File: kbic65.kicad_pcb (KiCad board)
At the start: 2 copper layers, 141 parts, among them U1 ProMicro

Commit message: Added and updated footprints
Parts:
- added MX_BKSLSH2(ISO_Enter): MX-NoLED, MX_Only:MXOnly-ISO-ROTATED-ReversedStabilizers-NoLED, F.Cu at (287.3, 60.3)
- added MX_CpsLck2: MX-NoLED, MX_Only:MXOnly-1.25U-NoLED, F.Cu at (25.4, 69.8)
- added MX_Enter2(ISO_Hash): MX-NoLED, MX_Only:MXOnly-1U-NoLED, F.Cu at (265.9, 69.8)
- added MX_LShift2: MX-NoLED, MX_Only:MXOnly-2.25U-NoLED, F.Cu at (34.9, 88.9)
- added MX_RAlt2: MX-NoLED, MX_Only:MXOnly-1.25U-NoLED, F.Cu at (211.1, 108.0)
- added MX_RAlt3: MX-NoLED, MX_Only:MXOnly-1.25U-NoLED, F.Cu at (215.9, 108.0)
- added MX_RWin2(RCtrl2): MX-NoLED, MX_Only:MXOnly-1.25U-NoLED, F.Cu at (239.7, 108.0)
- added MX_Space2: MX-NoLED, MX_Only:MXOnly-6U-Centered-NoLED, F.Cu at (142.1, 108.0)
- MX_BKSLSH1: footprint MX_Only:MXOnly-1U-NoLED -> MX_Only:MXOnly-1.5U-NoLED
- MX_Enter1: footprint MX_Only:MXOnly-1U-NoLED -> MX_Only:MXOnly-2.25U-NoLED

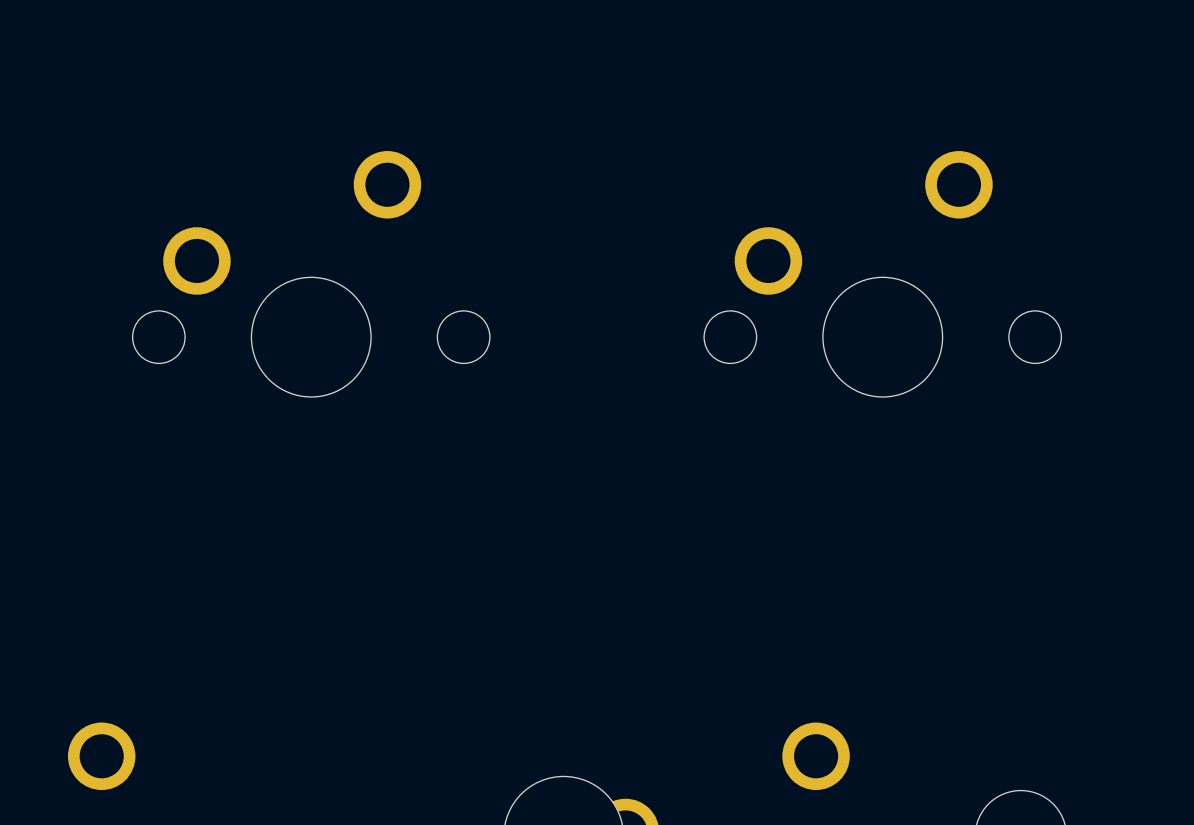
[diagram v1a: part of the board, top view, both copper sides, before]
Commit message: Added and updated footprints
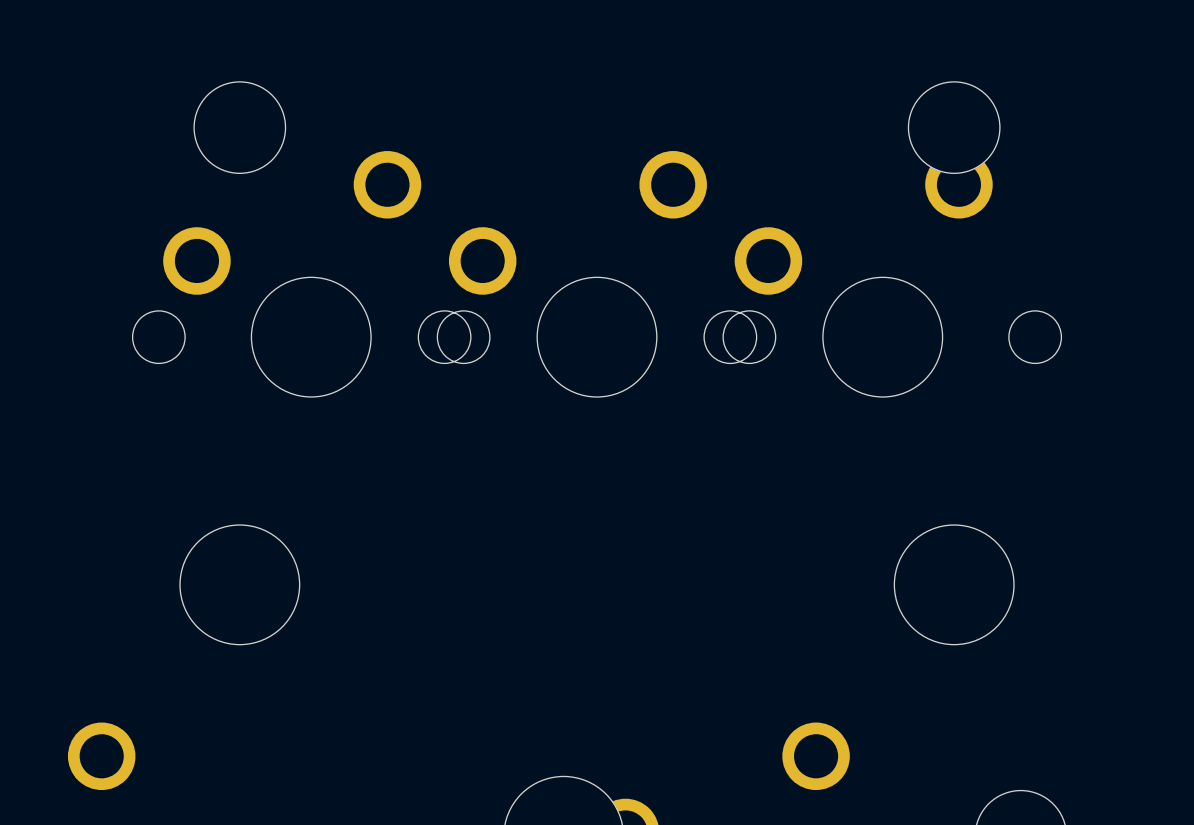
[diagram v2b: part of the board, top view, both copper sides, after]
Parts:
- added MX_BkSp2(RegBkSp): MX-NoLED, MX_Only:MXOnly-2U-NoLED, F.Cu at (280.2, 31.8)
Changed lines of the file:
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@@
     (tracks 0)
     (zones 0)
-    (modules 149)
+    (modules 150)
     (nets 95)
   )
@@
     (add_net ROW8)
   )
+  (module MX_Only:MXOnly-2U-NoLED (layer F.Cu)
+    (at 280.19375 31.75)
+    (fp_text reference "MX_BkSp2(RegBkSp)" (at 0 3.175) (layer Dwgs.User)
+      (effects (font (size 1 1) (thickness 0.15)))
+    )
+    (fp_text value MX-NoLED (at 0 -7.9375) (layer Dwgs.User)
+      (effects (font (size 1 1) (thickness 0.15)))
+    )
+    (fp_line (start -19.05 9.525) (end -19.05 -9.525) (layer Dwgs.User) (width 0.15))
+    (fp_line (start -19.05 9.525) (end 19.05 9.525) (layer Dwgs.User) (width 0.15))
+    (fp_line (start 19.05 -9.525) (end 19.05 9.525) (layer Dwgs.User) (width 0.15))
+    (fp_line (start -19.05 -9.525) (end 19.05 -9.525) (layer Dwgs.User) (width 0.15))
+    (fp_line (start -7 -7) (end -7 -5) (layer Dwgs.User) (width 0.15))
+    (fp_line (start -5 -7) (end -7 -7) (layer Dwgs.User) (width 0.15))
+    (fp_line (start -7 7) (end -5 7) (layer Dwgs.User) (width 0.15))
+    (fp_line (start -7 5) (end -7 7) (layer Dwgs.User) (width 0.15))
+    (fp_line (start 7 7) (end 7 5) (layer Dwgs.User) (width 0.15))
+    (fp_line (start 5 7) (end 7 7) (layer Dwgs.User) (width 0.15))
+    (fp_line (start 7 -7) (end 7 -5) (layer Dwgs.User) (width 0.15))
+    (fp_line (start 5 -7) (end 7 -7) (layer Dwgs.User) (width 0.15))
+    (pad 2 thru_hole circle (at 2.54 -5.08) (size 2.25 2.25) (drill 1.47) (layers *.Cu B.Mask)
+      (net 20 "Net-(D_BkSp1-Pad2)"))
+    (pad "" np_thru_hole circle (at 0 0) (size 3.9878 3.9878) (drill 3.9878) (layers *.Cu *.Mask))
+    (pad 1 thru_hole circle (at -3.81 -2.54) (size 2.25 2.25) (drill 1.47) (layers *.Cu B.Mask)
+      (net 86 COL6))
+    (pad "" np_thru_hole circle (at -5.08 0 48.0996) (size 1.75 1.75) (drill 1.75) (layers *.Cu *.Mask))
+    (pad "" np_thru_hole circle (at 5.08 0 48.0996) (size 1.75 1.75) (drill 1.75) (layers *.Cu *.Mask))
+    (pad "" np_thru_hole circle (at -11.90625 -6.985) (size 3.048 3.048) (drill 3.048) (layers *.Cu *.Mask))
+    (pad "" np_thru_hole circle (at 11.90625 -6.985) (size 3.048 3.048) (drill 3.048) (layers *.Cu *.Mask))
+    (pad "" np_thru_hole circle (at -11.90625 8.255) (size 3.9878 3.9878) (drill 3.9878) (layers *.Cu *.Mask))
+    (pad "" np_thru_hole circle (at 11.90625 8.255) (size 3.9878 3.9878) (drill 3.9878) (layers *.Cu *.Mask))
+  )
   (module MX_Only:MXOnly-ISO-ROTATED-ReversedStabilizers-NoLED (layer F.Cu)

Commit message: Redrew schematic with all extra footprints
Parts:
- renumbered MX_CpsLck2 to MX_CpsLck2(Stepped), MX_LShift2 to MX_LShift2(ANSI)
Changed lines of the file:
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@@
   (module MX_Only:MXOnly-1.25U-NoLED (layer F.Cu)
     (at 25.4 69.85)
-    (fp_text reference MX_CpsLck2 (at 0 3.175) (layer Dwgs.User)
+    (fp_text reference "MX_CpsLck2(Stepped)" (at 0 3.175) (layer Dwgs.User)
       (effects (font (size 1 1) (thickness 0.15)))
     )
@@
   (module MX_Only:MXOnly-2.25U-NoLED (layer F.Cu)
     (at 34.925 88.9)
-    (fp_text reference MX_LShift2 (at 0 3.175) (layer Dwgs.User)
+    (fp_text reference "MX_LShift2(ANSI)" (at 0 3.175) (layer Dwgs.User)
       (effects (font (size 1 1) (thickness 0.15)))
     )

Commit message: Changed layout to top windows and rearranging diodes
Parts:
- removed MX_BKSLSH2(ISO_Enter): MX-NoLED, MX_Only:MXOnly-ISO-ROTATED-ReversedStabilizers-NoLED
- removed MX_BkSp2(RegBkSp): MX-NoLED, MX_Only:MXOnly-2U-NoLED
- removed MX_CpsLck2(Stepped), MX_LShift1, MX_RAlt2, MX_RAlt3, MX_RWin2(RCtrl2): MX-NoLED, MX_Only:MXOnly-1.25U-NoLED
- removed MX_Enter2(ISO_Hash), MX_RAlt1: MX-NoLED, MX_Only:MXOnly-1U-NoLED
- removed MX_LShift2(ANSI): MX-NoLED, MX_Only:MXOnly-2.25U-NoLED
- removed MX_Space1: MX-NoLED, MX_Only:MXOnly-6.25U-NoLED
- removed MX_Space2: MX-NoLED, MX_Only:MXOnly-6U-Centered-NoLED
- added MX_BkSlash2_ISO_Enter1: MX-NoLED, MX_Only:MXOnly-ISO-ROTATED-ReversedStabilizers-NoLED, F.Cu at (346.1, 98.4)
- added MX_BkSp3_2u1: MX-NoLED, MX_Only:MXOnly-2U-NoLED, F.Cu at (338.9, 69.8)
- added MX_CpsLck2_Stepped1: MX-NoLED, MX_Only:MXOnly-1.25U-NoLED, F.Cu at (84.1, 108.0)
- added MX_Enter2_ISO_Hash1: MX-NoLED, MX_Only:MXOnly-1U-NoLED, F.Cu at (324.6, 108.0)
- added MX_LShift_ANSI1: MX-NoLED, MX_Only:MXOnly-2.25U-NoLED, F.Cu at (93.7, 127.0)
- added MX_LShift_ISO1: MX-NoLED, MX_Only:MXOnly-1.25U-NoLED, F.Cu at (84.1, 127.0)
- added MX_RAlt1_1u1: MX-NoLED, MX_Only:MXOnly-1U-NoLED, F.Cu at (272.3, 146.1)
- added MX_RAlt2_1.25u_6u_space1: MX-NoLED, MX_Only:MXOnly-1.25U-NoLED, F.Cu at (269.9, 146.1)
- added MX_RAlt3_1.25u_6.25u_space1: MX-NoLED, MX_Only:MXOnly-1.25U-NoLED, F.Cu at (274.6, 146.1)
- added MX_RWin2_1.25u_RCtrl1: MX-NoLED, MX_Only:MXOnly-1U-NoLED, F.Cu at (298.4, 146.1)
- added MX_Space1_6.25u1: MX-NoLED, MX_Only:MXOnly-6.25U-NoLED, F.Cu at (203.2, 146.1)
- added MX_Space2_6u1: MX-NoLED, MX_Only:MXOnly-6U-Centered-NoLED, F.Cu at (200.8, 146.1)
- moved D_PgDn1 424.5 mm to (396.9, 31.8), turned to 270 degrees
- moved D_Right1 419.5 mm to (401.6, 31.8), turned to 270 degrees
- moved D_PgUp1 416.6 mm to (392.1, 31.8), turned to 270 degrees
- moved D_Del1 401.9 mm to (387.4, 31.8), turned to 270 degrees
- moved D_Up1 387.2 mm to (368.3, 31.8), turned to 270 degrees
- moved D_Down1 381.8 mm to (373.1, 31.8), turned to 270 degrees
- moved D_Tilde1 375.8 mm to (382.6, 31.8), turned to 270 degrees
- moved D_Enter1 370.7 mm to (331.6, -10.5), turned to 270 degrees
- moved D_BKSLSH1 368.3 mm to (363.5, 31.8), turned to 270 degrees
- moved D_SemiCol1 368.2 mm to (327.8, -10.5), turned to 270 degrees
- moved D_K1 365.8 mm to (324.0, -10.5), turned to 270 degrees
- moved D_H1 363.4 mm to (320.2, -10.5), turned to 270 degrees
- moved D_@1 362.3 mm to (327.8, -20.3), turned to 270 degrees
- moved D_F1 361.1 mm to (316.4, -10.5), turned to 270 degrees
- moved D_L1 359.6 mm to (324.0, -20.3), turned to 270 degrees
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- renumbered MX_BKSLSH1 to MX_BkSlsh1

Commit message: Changed diode to row2col instead to make better wiring, rearranging diode footprints
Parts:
- moved D_1 221.6 mm to (110.3, 47.6)
- moved D_Tab1 202.5 mm to (122.2, 47.6)
- moved D_A1 194.8 mm to (126.2, 47.6)
- moved D_3 194.1 mm to (146.1, 46.0)
- moved D_Esc1 188.0 mm to (114.3, 47.6)
- moved D_CpsLck1 187.8 mm to (130.2, 47.6)
- moved D_Q1 183.8 mm to (118.3, 47.6)
- moved D_ISO_BKSLSH1 179.6 mm to (134.1, 47.6)
- moved D_W1 172.7 mm to (158.0, 46.0)
- moved D_5 167.6 mm to (181.8, 43.7)
- moved D_D1 164.6 mm to (161.9, 46.0)
- moved D_2 160.8 mm to (150.0, 46.0)
- moved D_S1 157.2 mm to (165.9, 46.0)
- moved D_E1 155.6 mm to (154.0, 46.0)
- moved D_X1 148.6 mm to (169.9, 46.0)
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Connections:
- D_0 pad 1: ROW1 -> COL5
- D_1 pad 1: ROW0 -> COL0
- D_2 pad 1: ROW1 -> COL1
- D_3 pad 1: ROW0 -> COL1
- D_4 pad 1: ROW1 -> COL2
- D_5 pad 1: ROW0 -> COL2
- D_6 pad 1: ROW1 -> COL3
- D_7 pad 1: ROW0 -> COL3
- D_8 pad 1: ROW1 -> COL4
- D_9 pad 1: ROW0 -> COL4
- D_@1 pad 1: ROW4 -> COL5
- D_A1 pad 1: ROW4 -> COL0
- D_B1 pad 1: ROW7 -> COL3
- D_BKSLSH1 pad 1: ROW2 -> COL6
- D_BkSp1 pad 1: ROW0 -> COL6
- D_BkSp2 pad 1: ROW1 -> COL7
- D_C1 pad 1: ROW7 -> COL2
- D_Comma1 pad 1: ROW6 -> COL4
- D_CpsLck1 pad 1: ROW5 -> COL0
- D_D1 pad 1: ROW4 -> COL1
- D_Del1 pad 1: ROW3 -> COL7
- D_Dot1 pad 1: ROW7 -> COL5
- D_Down1 pad 1: ROW7 -> COL7
- D_E1 pad 1: ROW2 -> COL1
- D_Enter1 pad 1: ROW5 -> COL6
- D_Equal1 pad 1: ROW1 -> COL6
- D_Esc1 pad 1: ROW1 -> COL0
- D_F1 pad 1: ROW5 -> COL2
- D_FwdSlsh1 pad 1: ROW6 -> COL5
- D_G1 pad 1: ROW4 -> COL2
- D_H1 pad 1: ROW5 -> COL3
- D_Hyphen1 pad 1: ROW0 -> COL5
- D_I1 pad 1: ROW3 -> COL4
- D_ISO_BKSLSH1 pad 1: ROW6 -> COL0
- D_J1 pad 1: ROW4 -> COL3
- D_K1 pad 1: ROW5 -> COL4
- D_L1 pad 1: ROW4 -> COL4
- D_LAlt1 pad 1: ROW8 -> COL2
- D_LBKT1 pad 1: ROW2 -> COL5
- D_LCtrl1 pad 1: ROW8 -> COL0
- D_LShift1 pad 1: ROW7 -> COL0
- D_LWin1 pad 1: ROW8 -> COL1
- D_Left1 pad 1: ROW8 -> COL7
- D_M1 pad 1: ROW7 -> COL4
- D_N1 pad 1: ROW6 -> COL3
- D_O1 pad 1: ROW2 -> COL4
- D_P1 pad 1: ROW3 -> COL5
- D_PgDn1 pad 1: ROW5 -> COL7
- D_PgUp1 pad 1: ROW4 -> COL7
- D_Q1 pad 1: ROW2 -> COL0
- D_R1 pad 1: ROW3 -> COL2
- D_RAlt1 pad 1: ROW8 -> COL4
- D_RBKT1 pad 1: ROW3 -> COL6
- D_RCtrl1 pad 1: ROW8 -> COL6
- D_RShift1 pad 1: ROW7 -> COL6
- D_RWin1 pad 1: ROW8 -> COL5
- D_Right1 pad 1: ROW6 -> COL7
- D_S1 pad 1: ROW5 -> COL1
- D_SemiCol1 pad 1: ROW5 -> COL5
- D_Space1 pad 1: ROW8 -> COL3
- D_T1 pad 1: ROW2 -> COL2
- D_Tab1 pad 1: ROW3 -> COL0
- D_Tilde1 pad 1: ROW0 -> COL7
- D_U1 pad 1: ROW2 -> COL3
- D_Up1 pad 1: ROW6 -> COL6
- D_V1 pad 1: ROW6 -> COL2
- D_W1 pad 1: ROW3 -> COL1
- D_X1 pad 1: ROW6 -> COL1
- D_Y1 pad 1: ROW3 -> COL3
- D_Z1 pad 1: ROW7 -> COL1
- MX_0 pad 1: COL5 -> Net-(D_0-Pad2)
- MX_0 pad 2: Net-(D_0-Pad2) -> ROW1
- MX_1 pad 1: COL0 -> Net-(D_1-Pad2)
- MX_1 pad 2: Net-(D_1-Pad2) -> ROW0
- MX_2 pad 1: COL1 -> Net-(D_2-Pad2)
- MX_2 pad 2: Net-(D_2-Pad2) -> ROW1
- MX_3 pad 1: COL1 -> Net-(D_3-Pad2)
- MX_3 pad 2: Net-(D_3-Pad2) -> ROW0
- MX_4 pad 1: COL2 -> Net-(D_4-Pad2)
- MX_4 pad 2: Net-(D_4-Pad2) -> ROW1
- MX_5 pad 1: COL2 -> Net-(D_5-Pad2)
- MX_5 pad 2: Net-(D_5-Pad2) -> ROW0
- MX_6 pad 1: COL3 -> Net-(D_6-Pad2)
- MX_6 pad 2: Net-(D_6-Pad2) -> ROW1
- MX_7 pad 1: COL3 -> Net-(D_7-Pad2)
- MX_7 pad 2: Net-(D_7-Pad2) -> ROW0
- MX_8 pad 1: COL4 -> Net-(D_8-Pad2)
- MX_8 pad 2: Net-(D_8-Pad2) -> ROW1
- MX_9 pad 1: COL4 -> Net-(D_9-Pad2)
- MX_9 pad 2: Net-(D_9-Pad2) -> ROW0
- MX_@1 pad 1: COL5 -> Net-(D_@1-Pad2)
- MX_@1 pad 2: Net-(D_@1-Pad2) -> ROW4
- MX_A1 pad 1: COL0 -> Net-(D_A1-Pad2)
- MX_A1 pad 2: Net-(D_A1-Pad2) -> ROW4
- MX_B1 pad 1: COL3 -> Net-(D_B1-Pad2)
- MX_B1 pad 2: Net-(D_B1-Pad2) -> ROW7
- MX_BkSlash2_ISO_Enter1 pad 1: COL6 -> Net-(D_BKSLSH1-Pad2)
- MX_BkSlash2_ISO_Enter1 pad 2: Net-(D_BKSLSH1-Pad2) -> ROW2
- MX_BkSlsh1 pad 1: COL6 -> Net-(D_BKSLSH1-Pad2)
- MX_BkSlsh1 pad 2: Net-(D_BKSLSH1-Pad2) -> ROW2
- MX_BkSp1 pad 1: COL6 -> Net-(D_BkSp1-Pad2)
- MX_BkSp1 pad 2: Net-(D_BkSp1-Pad2) -> ROW0
- MX_BkSp2 pad 1: COL7 -> Net-(D_BkSp2-Pad2)
- MX_BkSp2 pad 2: Net-(D_BkSp2-Pad2) -> ROW1
- MX_BkSp3_2u1 pad 1: COL6 -> Net-(D_BkSp1-Pad2)
- MX_BkSp3_2u1 pad 2: Net-(D_BkSp1-Pad2) -> ROW0
- MX_C1 pad 1: COL2 -> Net-(D_C1-Pad2)
- MX_C1 pad 2: Net-(D_C1-Pad2) -> ROW7
- MX_Comma1 pad 1: COL4 -> Net-(D_Comma1-Pad2)
- MX_Comma1 pad 2: Net-(D_Comma1-Pad2) -> ROW6
- MX_CpsLck1 pad 1: COL0 -> Net-(D_CpsLck1-Pad2)
- MX_CpsLck1 pad 2: Net-(D_CpsLck1-Pad2) -> ROW5
- MX_CpsLck2_Stepped1 pad 1: COL0 -> Net-(D_CpsLck1-Pad2)
- MX_CpsLck2_Stepped1 pad 2: Net-(D_CpsLck1-Pad2) -> ROW5
- MX_D1 pad 1: COL1 -> Net-(D_D1-Pad2)
- MX_D1 pad 2: Net-(D_D1-Pad2) -> ROW4
- MX_Del1 pad 1: COL7 -> Net-(D_Del1-Pad2)
- MX_Del1 pad 2: Net-(D_Del1-Pad2) -> ROW3
- MX_Dot1 pad 1: COL5 -> Net-(D_Dot1-Pad2)
- MX_Dot1 pad 2: Net-(D_Dot1-Pad2) -> ROW7
- MX_Down1 pad 1: COL7 -> Net-(D_Down1-Pad2)
- MX_Down1 pad 2: Net-(D_Down1-Pad2) -> ROW7
- MX_E1 pad 1: COL1 -> Net-(D_E1-Pad2)
- MX_E1 pad 2: Net-(D_E1-Pad2) -> ROW2
- MX_Enter1 pad 1: COL6 -> Net-(D_Enter1-Pad2)
- MX_Enter1 pad 2: Net-(D_Enter1-Pad2) -> ROW5
- MX_Enter2_ISO_Hash1 pad 1: COL6 -> Net-(D_Enter1-Pad2)
- MX_Enter2_ISO_Hash1 pad 2: Net-(D_Enter1-Pad2) -> ROW5
- MX_Equal1 pad 1: COL6 -> Net-(D_Equal1-Pad2)
- MX_Equal1 pad 2: Net-(D_Equal1-Pad2) -> ROW1
- MX_Esc1 pad 1: COL0 -> Net-(D_Esc1-Pad2)
- MX_Esc1 pad 2: Net-(D_Esc1-Pad2) -> ROW1
- MX_F1 pad 1: COL2 -> Net-(D_F1-Pad2)
- MX_F1 pad 2: Net-(D_F1-Pad2) -> ROW5
- MX_FwdSlsh1 pad 1: COL5 -> Net-(D_FwdSlsh1-Pad2)
- MX_FwdSlsh1 pad 2: Net-(D_FwdSlsh1-Pad2) -> ROW6
- MX_G1 pad 1: COL2 -> Net-(D_G1-Pad2)
- MX_G1 pad 2: Net-(D_G1-Pad2) -> ROW4
- MX_H1 pad 1: COL3 -> Net-(D_H1-Pad2)
- MX_H1 pad 2: Net-(D_H1-Pad2) -> ROW5
- MX_Hyphen1 pad 1: COL5 -> Net-(D_Hyphen1-Pad2)
- MX_Hyphen1 pad 2: Net-(D_Hyphen1-Pad2) -> ROW0
- MX_I1 pad 1: COL4 -> Net-(D_I1-Pad2)
- MX_I1 pad 2: Net-(D_I1-Pad2) -> ROW3
- MX_ISO_BKSLSH1 pad 1: COL0 -> Net-(D_ISO_BKSLSH1-Pad2)
- MX_ISO_BKSLSH1 pad 2: Net-(D_ISO_BKSLSH1-Pad2) -> ROW6
- MX_J1 pad 1: COL3 -> Net-(D_J1-Pad2)
- MX_J1 pad 2: Net-(D_J1-Pad2) -> ROW4
- MX_K1 pad 1: COL4 -> Net-(D_K1-Pad2)
- MX_K1 pad 2: Net-(D_K1-Pad2) -> ROW5
- MX_L1 pad 1: COL4 -> Net-(D_L1-Pad2)
- MX_L1 pad 2: Net-(D_L1-Pad2) -> ROW4
- MX_LAlt1 pad 1: COL2 -> Net-(D_LAlt1-Pad2)
- MX_LAlt1 pad 2: Net-(D_LAlt1-Pad2) -> ROW8
- MX_LBKT1 pad 1: COL5 -> Net-(D_LBKT1-Pad2)
- MX_LBKT1 pad 2: Net-(D_LBKT1-Pad2) -> ROW2
- MX_LCtrl1 pad 1: COL0 -> Net-(D_LCtrl1-Pad2)
- MX_LCtrl1 pad 2: Net-(D_LCtrl1-Pad2) -> ROW8
- MX_LShift_ANSI1 pad 1: COL0 -> Net-(D_LShift1-Pad2)
- MX_LShift_ANSI1 pad 2: Net-(D_LShift1-Pad2) -> ROW7
- MX_LShift_ISO1 pad 1: COL0 -> Net-(D_LShift1-Pad2)
- MX_LShift_ISO1 pad 2: Net-(D_LShift1-Pad2) -> ROW7
- MX_LWin1 pad 1: COL1 -> Net-(D_LWin1-Pad2)
- MX_LWin1 pad 2: Net-(D_LWin1-Pad2) -> ROW8
- MX_Left1 pad 1: COL7 -> Net-(D_Left1-Pad2)
- MX_Left1 pad 2: Net-(D_Left1-Pad2) -> ROW8
- MX_M1 pad 1: COL4 -> Net-(D_M1-Pad2)
- MX_M1 pad 2: Net-(D_M1-Pad2) -> ROW7
- MX_N1 pad 1: COL3 -> Net-(D_N1-Pad2)
- MX_N1 pad 2: Net-(D_N1-Pad2) -> ROW6
- MX_O1 pad 1: COL4 -> Net-(D_O1-Pad2)
- MX_O1 pad 2: Net-(D_O1-Pad2) -> ROW2
- MX_P1 pad 1: COL5 -> Net-(D_P1-Pad2)
- MX_P1 pad 2: Net-(D_P1-Pad2) -> ROW3
- MX_PgDn1 pad 1: COL7 -> Net-(D_PgDn1-Pad2)
- MX_PgDn1 pad 2: Net-(D_PgDn1-Pad2) -> ROW5
- MX_PgUp1 pad 1: COL7 -> Net-(D_PgUp1-Pad2)
- MX_PgUp1 pad 2: Net-(D_PgUp1-Pad2) -> ROW4
- MX_Q1 pad 1: COL0 -> Net-(D_Q1-Pad2)
- MX_Q1 pad 2: Net-(D_Q1-Pad2) -> ROW2
- MX_R1 pad 1: COL2 -> Net-(D_R1-Pad2)
- MX_R1 pad 2: Net-(D_R1-Pad2) -> ROW3
- MX_RAlt1_1u1 pad 1: Net-(MX_RAlt1_1u1-Pad1) -> Net-(D_RAlt1-Pad2)
- MX_RAlt1_1u1 pad 2: Net-(D_RAlt1-Pad2) -> ROW8
- MX_RAlt2_1.25u_6u_space1 pad 1: Net-(MX_RAlt1_1u1-Pad1) -> Net-(D_RAlt1-Pad2)
- MX_RAlt2_1.25u_6u_space1 pad 2: Net-(D_RAlt1-Pad2) -> ROW8
- MX_RAlt3_1.25u_6.25u_space1 pad 1: Net-(MX_RAlt1_1u1-Pad1) -> Net-(D_RAlt1-Pad2)
- MX_RAlt3_1.25u_6.25u_space1 pad 2: Net-(D_RAlt1-Pad2) -> ROW8
- MX_RBKT1 pad 1: COL6 -> Net-(D_RBKT1-Pad2)
- MX_RBKT1 pad 2: Net-(D_RBKT1-Pad2) -> ROW3
- MX_RCtrl1 pad 1: COL6 -> Net-(D_RCtrl1-Pad2)
- MX_RCtrl1 pad 2: Net-(D_RCtrl1-Pad2) -> ROW8
- MX_RShift1 pad 1: COL6 -> Net-(D_RShift1-Pad2)
- MX_RShift1 pad 2: Net-(D_RShift1-Pad2) -> ROW7
- MX_RWin1 pad 1: COL5 -> Net-(D_RWin1-Pad2)
- MX_RWin1 pad 2: Net-(D_RWin1-Pad2) -> ROW8
- MX_RWin2_1.25u_RCtrl1 pad 1: COL5 -> Net-(D_RWin1-Pad2)
- MX_RWin2_1.25u_RCtrl1 pad 2: Net-(D_RWin1-Pad2) -> ROW8
- MX_Right1 pad 1: COL7 -> Net-(D_Right1-Pad2)
- MX_Right1 pad 2: Net-(D_Right1-Pad2) -> ROW6
- MX_S1 pad 1: COL1 -> Net-(D_S1-Pad2)
- MX_S1 pad 2: Net-(D_S1-Pad2) -> ROW5
- MX_SemiCol1 pad 1: COL5 -> Net-(D_SemiCol1-Pad2)
- MX_SemiCol1 pad 2: Net-(D_SemiCol1-Pad2) -> ROW5
- MX_Space1_6.25u1 pad 1: COL3 -> Net-(D_Space1-Pad2)
- MX_Space1_6.25u1 pad 2: Net-(D_Space1-Pad2) -> ROW8
- MX_Space2_6u1 pad 1: COL3 -> Net-(D_Space1-Pad2)
- MX_Space2_6u1 pad 2: Net-(D_Space1-Pad2) -> ROW8
- MX_T1 pad 1: COL2 -> Net-(D_T1-Pad2)
- MX_T1 pad 2: Net-(D_T1-Pad2) -> ROW2
- MX_Tab1 pad 1: COL0 -> Net-(D_Tab1-Pad2)
- MX_Tab1 pad 2: Net-(D_Tab1-Pad2) -> ROW3
- MX_Tilde1 pad 1: COL7 -> Net-(D_Tilde1-Pad2)
- MX_Tilde1 pad 2: Net-(D_Tilde1-Pad2) -> ROW0
- MX_U1 pad 1: COL3 -> Net-(D_U1-Pad2)
- MX_U1 pad 2: Net-(D_U1-Pad2) -> ROW2
- MX_Up1 pad 1: COL6 -> Net-(D_Up1-Pad2)
- MX_Up1 pad 2: Net-(D_Up1-Pad2) -> ROW6
- MX_V1 pad 1: COL2 -> Net-(D_V1-Pad2)
- MX_V1 pad 2: Net-(D_V1-Pad2) -> ROW6
- MX_W1 pad 1: COL1 -> Net-(D_W1-Pad2)
- MX_W1 pad 2: Net-(D_W1-Pad2) -> ROW3
- MX_X1 pad 1: COL1 -> Net-(D_X1-Pad2)
- MX_X1 pad 2: Net-(D_X1-Pad2) -> ROW6
- MX_Y1 pad 1: COL3 -> Net-(D_Y1-Pad2)
- MX_Y1 pad 2: Net-(D_Y1-Pad2) -> ROW3
- MX_Z1 pad 1: COL1 -> Net-(D_Z1-Pad2)
- MX_Z1 pad 2: Net-(D_Z1-Pad2) -> ROW7

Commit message: Rearranged diodes for wiring
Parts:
- moved D_LBKT1 28.1 mm to (321.5, 50.0)
- moved D_U1 26.4 mm to (250.0, 50.8)
- moved D_O1 25.9 mm to (285.8, 46.8)
- moved D_E1 25.1 mm to (178.6, 50.8)
- moved D_T1 24.8 mm to (214.3, 46.8)
- moved D_Q1 24.6 mm to (142.9, 46.8)
- moved D_LWin1 19.6 mm to (158.8, 50.8)
- moved D_LAlt1 19.3 mm to (194.5, 46.8)
- moved D_@1 18.5 mm to (317.5, 50.0)
- moved D_BkSp1 18.5 mm to (353.2, 46.8)
- moved D_RBKT1 18.5 mm to (345.3, 46.8)
- moved D_Dot1 17.5 mm to (305.6, 50.0)
- moved D_RWin1 17.5 mm to (309.6, 50.0)
- moved D_RCtrl1 17.0 mm to (329.4, 46.8)
- moved D_Up1 17.0 mm to (337.3, 46.8)
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
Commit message: Rearranged rows on promicro footprint
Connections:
- U1 pad 10: ROW6 -> ROW2
- U1 pad 11: ROW7 -> ROW1
- U1 pad 12: ROW8 -> ROW0
- U1 pad 2: ROW0 -> ROW8
- U1 pad 5: ROW1 -> ROW7
- U1 pad 6: ROW2 -> ROW6
- U1 pad 7: ROW3 -> ROW5
- U1 pad 9: ROW5 -> ROW3
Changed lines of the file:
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@@
       (net 88 "Net-(U1-Pad24)"))
     (pad 12 thru_hole circle (at 13.97 7.3914) (size 1.7526 1.7526) (drill 1.0922) (layers *.Cu *.SilkS *.Mask)
-      (net 47 ROW8))
+      (net 4 ROW0))
     (pad 23 thru_hole circle (at -11.43 -7.3914) (size 1.7526 1.7526) (drill 1.0922) (layers *.Cu *.SilkS *.Mask)
       (net 89 "Net-(U1-Pad23)"))
@@
       (net 87 COL7))
     (pad 11 thru_hole circle (at 11.43 7.8486) (size 1.7526 1.7526) (drill 1.0922) (layers *.Cu *.SilkS *.Mask)
-      (net 17 ROW7))
+      (net 2 ROW1))
     (pad 10 thru_hole circle (at 8.89 7.3914) (size 1.7526 1.7526) (drill 1.0922) (layers *.Cu *.SilkS *.Mask)
-      (net 24 ROW6))
+      (net 19 ROW2))
     (pad 9 thru_hole circle (at 6.35 7.8486) (size 1.7526 1.7526) (drill 1.0922) (layers *.Cu *.SilkS *.Mask)
-      (net 26 ROW5))
+      (net 29 ROW3))
     (pad 8 thru_hole circle (at 3.81 7.3914) (size 1.7526 1.7526) (drill 1.0922) (layers *.Cu *.SilkS *.Mask)
       (net 14 ROW4))
     (pad 7 thru_hole circle (at 1.27 7.8486) (size 1.7526 1.7526) (drill 1.0922) (layers *.Cu *.SilkS *.Mask)
-      (net 29 ROW3))
+      (net 26 ROW5))
     (pad 6 thru_hole circle (at -1.27 7.3914) (size 1.7526 1.7526) (drill 1.0922) (layers *.Cu *.SilkS *.Mask)
-      (net 19 ROW2))
+      (net 24 ROW6))
     (pad 5 thru_hole circle (at -3.81 7.8486) (size 1.7526 1.7526) (drill 1.0922) (layers *.Cu *.SilkS *.Mask)
-      (net 2 ROW1))
+      (net 17 ROW7))
     (pad 4 thru_hole circle (at -6.35 7.3914) (size 1.7526 1.7526) (drill 1.0922) (layers *.Cu *.SilkS *.Mask)
       (net 92 "Net-(U1-Pad4)"))
@@
       (net 93 "Net-(U1-Pad3)"))
     (pad 2 thru_hole circle (at -11.43 7.3914) (size 1.7526 1.7526) (drill 1.0922) (layers *.Cu *.SilkS *.Mask)
-      (net 4 ROW0))
+      (net 47 ROW8))
     (pad 1 thru_hole rect (at -13.97 7.8486) (size 1.7526 1.7526) (drill 1.0922) (layers *.Cu *.SilkS *.Mask)
       (net 94 "Net-(U1-Pad1)"))

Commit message: Simple arrangement of diodes
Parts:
- moved D_0 2.51 mm to (287.3, 49.2)
- moved D_@1 2.51 mm to (315.1, 49.2)
- moved D_BkSp2 2.51 mm to (354.8, 49.2)
- moved D_Del1 2.51 mm to (378.6, 49.2)
- moved D_Dot1 2.51 mm to (303.2, 49.2)
- moved D_Down1 2.51 mm to (362.7, 49.2)
- moved D_FwdSlsh1 2.51 mm to (311.1, 49.2)
- moved D_Hyphen1 2.51 mm to (291.3, 49.2)
- moved D_LBKT1 2.51 mm to (319.1, 49.2)
- moved D_Left1 2.51 mm to (358.8, 49.2)
- moved D_P1 2.51 mm to (295.3, 49.2)
- moved D_PgDn1 2.51 mm to (370.7, 49.2)
- moved D_PgUp1 2.51 mm to (374.6, 49.2)
- moved D_RWin1 2.51 mm to (307.2, 49.2)
- moved D_Right1 2.51 mm to (366.7, 49.2)
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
